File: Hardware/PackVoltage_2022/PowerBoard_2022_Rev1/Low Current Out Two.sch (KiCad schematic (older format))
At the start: 81 parts, among them Q10 BUK7M8R5-40HX, Q11 BUK7M8R5-40HX, Q12 BUK7M8R5-40HX, Q13 BUK7M8R5-40HX, Q14 BUK7M8R5-40HX, Q6 BUK7M8R5-40HX, Q7 BUK7M8R5-40HX, Q8 BUK7M8R5-40HX, Q9 BUK7M8R5-40HX, U22 LT1910, U23 LT1910, U24 LT1910, U25 LT1910, U26 INA281, U27 INA281, U28 INA281, U29 INA281, U30 INA281, U31 LT1910, U32 INA281, U33 LT1910, U34 LT1910, U35 LT1910, U36 LT1910, U37 INA281, U38 INA281, U39 INA281

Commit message: Made it to layout, found out about gnd via
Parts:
- renumbered C57 to C100, C58 to C101, C59 to C102, C60 to C103, C61 to C104, C62 to C105, C63 to C106, C64 to C107, C65 to C108, C66 to C109, C67 to C110, C50 to C93, C51 to C94, C52 to C95, C53 to C96, C54 to C97, C55 to C98, C56 to C99, D19 to D36, D20 to D37, D21 to D38, D22 to D39, D23 to D40, D24 to D41, D25 to D42, D26 to D43, D27 to D44, Q6 to Q14, Q7 to Q15, Q8 to Q16, Q9 to Q17, Q10 to Q18, Q11 to Q19, Q12 to Q20, Q13 to Q21, Q14 to Q22, R28 to R60, R29 to R61, R30 to R62, R31 to R63, R32 to R64, R33 to R65, R34 to R66, R35 to R67, R36 to R68, R37 to R69, R38 to R70, R39 to R71, R40 to R72, R41 to R73, R42 to R74, R43 to R75, R44 to R76, R45 to R77, R46 to R78, R47 to R79, R48 to R80, R49 to R81, R50 to R82, R51 to R83, R52 to R84, R53 to R85, R54 to R86, U22 to U48, U23 to U49, U24 to U50, U25 to U51, U26 to U52, U27 to U53, U28 to U54, U29 to U55, U30 to U56, U31 to U57, U32 to U58, U33 to U59, U34 to U60, U35 to U61, U36 to U62, U37 to U63, U38 to U64, U39 to U65

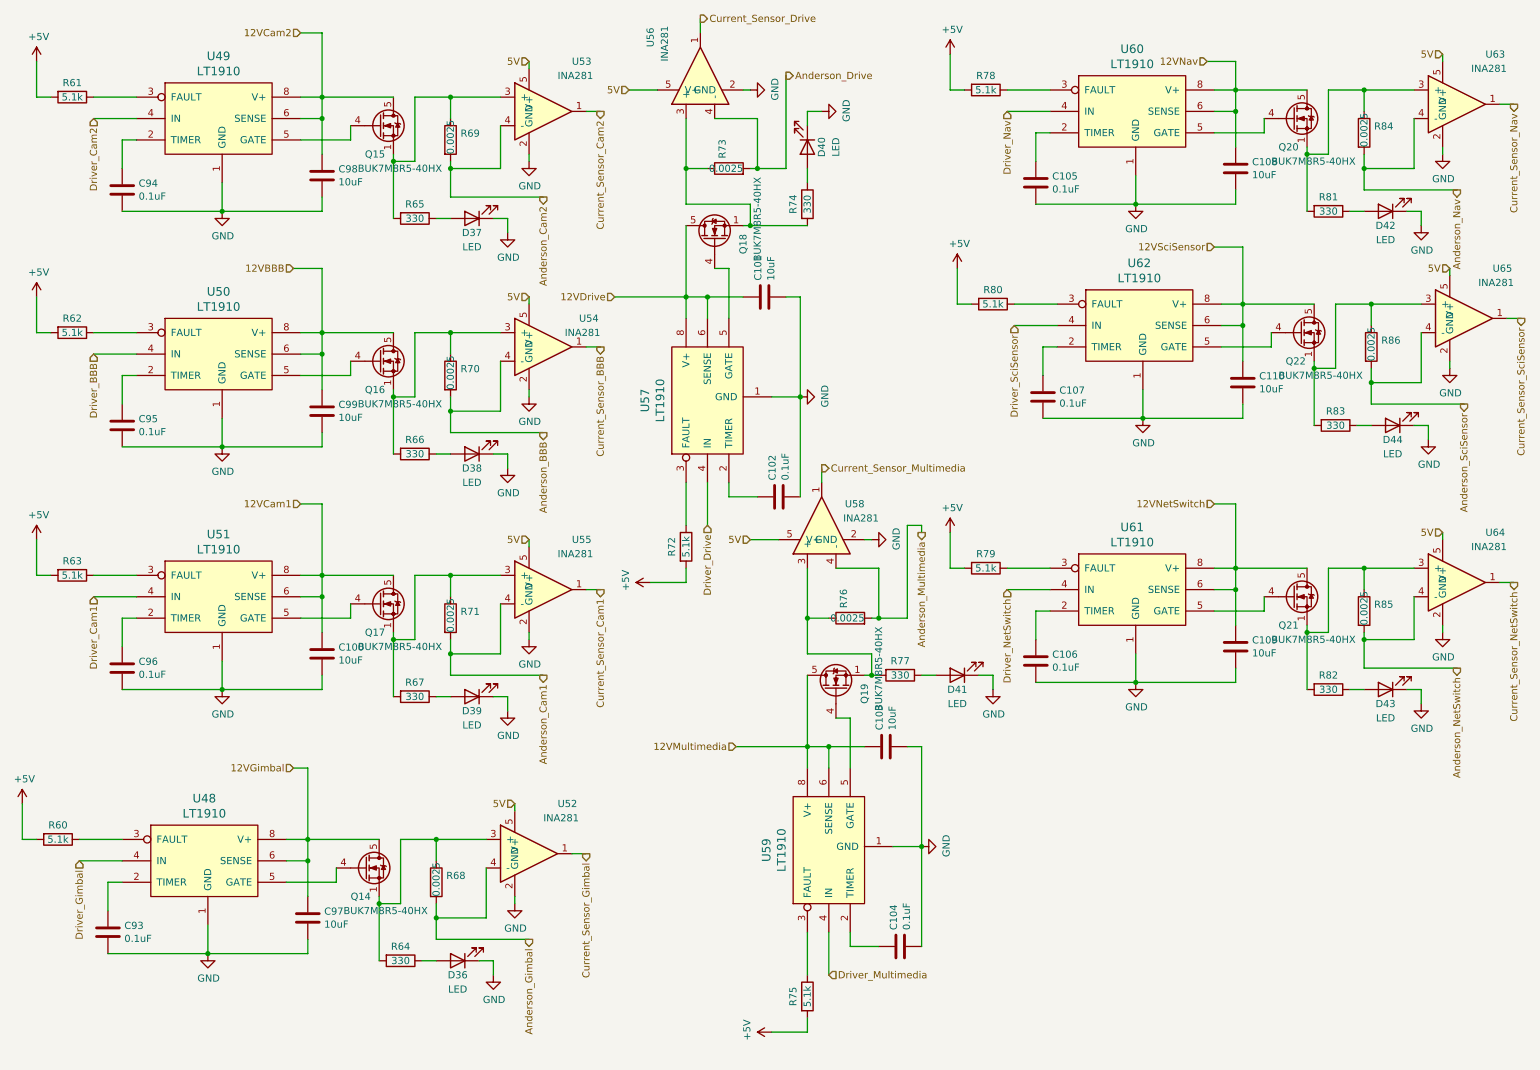
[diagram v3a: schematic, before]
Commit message: Organized  Stuff into groups and changed how we organize our board
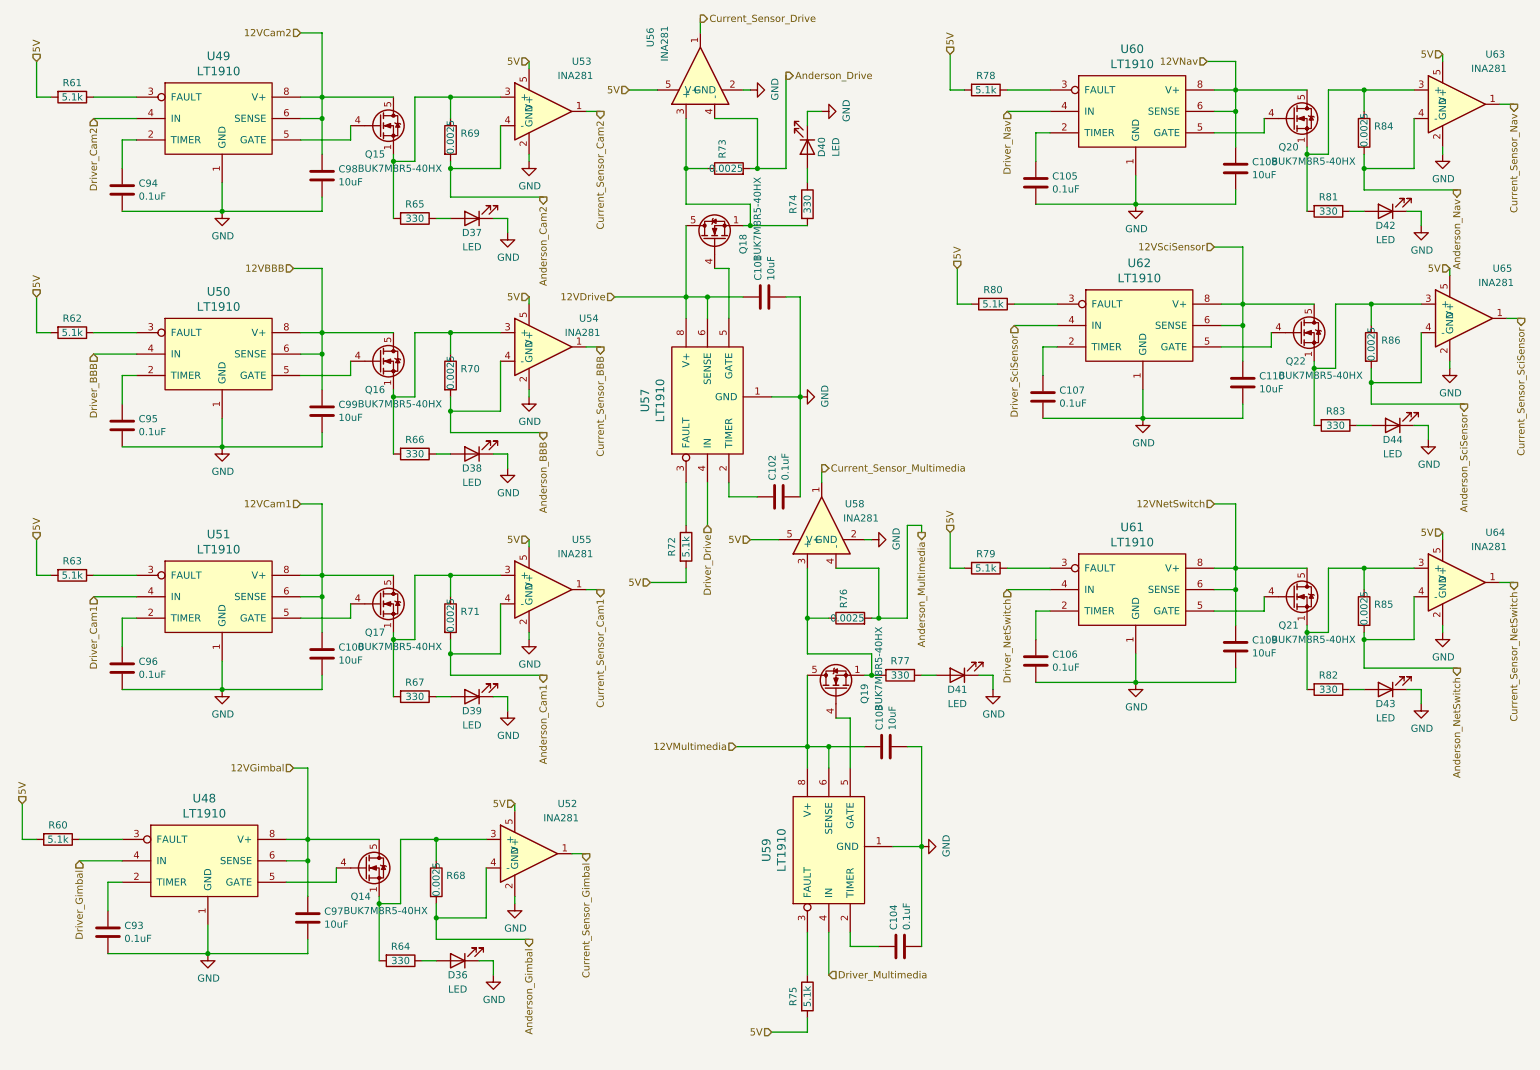
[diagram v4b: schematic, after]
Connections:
- net +5V is gone; now on net 5V: R60.2, R61.2, R62.2, R63.2, R72.2, R75.2, R78.2, R79.2, R80.2
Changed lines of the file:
@@
 EESchema Schematic File Version 4
-EELAYER 30 0
+LIBS:PowerBoard_2022_Rev1-cache
+EELAYER 26 0
 EELAYER END
 $Descr A4 11693 8268
@@
 Wire Wire Line
 	1100 2750 1400 2750
-$Comp
-L power:+5V #PWR?
-U 1 1 6179FA5B
-P 700 2500
-AR Path="/615D5992/6179FA5B" Ref="#PWR?"  Part="1"
-AR Path="/615D7BA0/6170B60A/6179FA5B" Ref="#PWR?"  Part="1"
-AR Path="/615D7BA0/6172F88A/6179FA5B" Ref="#PWR0124"  Part="1"
-F 0 "#PWR0124" H 700 2350 50  0001 C CNN
-F 1 "+5V" H 715 2673 50  0000 C CNN
-F 2 "" H 700 2500 50  0001 C CNN
-F 3 "" H 700 2500 50  0001 C CNN
-	1    700  2500
-	1    0    0    -1
-$EndComp
 Wire Wire Line
 	700  2500 700  2750
@@
 Wire Wire Line
 	1100 4450 1400 4450
-$Comp
-L power:+5V #PWR?
-U 1 1 6182162F
-P 700 4200
-AR Path="/615D5992/6182162F" Ref="#PWR?"  Part="1"
-AR Path="/615D7BA0/6170B60A/6182162F" Ref="#PWR?"  Part="1"
-AR Path="/615D7BA0/6172F88A/6182162F" Ref="#PWR0125"  Part="1"
-F 0 "#PWR0125" H 700 4050 50  0001 C CNN
-F 1 "+5V" H 715 4373 50  0000 C CNN
-F 2 "" H 700 4200 50  0001 C CNN
-F 3 "" H 700 4200 50  0001 C CNN
-	1    700  4200
-	1    0    0    -1
-$EndComp
 Wire Wire Line
 	700  4200 700  4450
@@
 Wire Wire Line
 	1100 1100 1400 1100
-$Comp
-L power:+5V #PWR?
-U 1 1 61833032
-P 700 850
-AR Path="/615D5992/61833032" Ref="#PWR?"  Part="1"
-AR Path="/615D7BA0/6170B60A/61833032" Ref="#PWR?"  Part="1"
-AR Path="/615D7BA0/6172F88A/61833032" Ref="#PWR0123"  Part="1"
-F 0 "#PWR0123" H 700 700 50  0001 C CNN
-F 1 "+5V" H 715 1023 50  0000 C CNN
-F 2 "" H 700 850 50  0001 C CNN
-F 3 "" H 700 850 50  0001 C CNN
-	1    700  850
-	1    0    0    -1
-$EndComp
 Wire Wire Line
 	700  850  700  1100
@@
 Wire Wire Line
 	7500 4400 7800 4400
-$Comp
-L power:+5V #PWR?
-U 1 1 61842604
-P 7100 4150
-AR Path="/615D5992/61842604" Ref="#PWR?"  Part="1"
-AR Path="/615D7BA0/6170B60A/61842604" Ref="#PWR?"  Part="1"
-AR Path="/615D7BA0/6172F88A/61842604" Ref="#PWR0146"  Part="1"
-F 0 "#PWR0146" H 7100 4000 50  0001 C CNN
-F 1 "+5V" H 7115 4323 50  0000 C CNN
-F 2 "" H 7100 4150 50  0001 C CNN
-F 3 "" H 7100 4150 50  0001 C CNN
-	1    7100 4150
-	1    0    0    -1
-$EndComp
 Wire Wire Line
 	7100 4150 7100 4400
@@
 Wire Wire Line
 	1000 6300 1300 6300
-$Comp
-L power:+5V #PWR?
-U 1 1 618D8DAA
-P 600 6050
-AR Path="/615D5992/618D8DAA" Ref="#PWR?"  Part="1"
-AR Path="/615D7BA0/6170B60A/618D8DAA" Ref="#PWR?"  Part="1"
-AR Path="/615D7BA0/6172F88A/618D8DAA" Ref="#PWR0122"  Part="1"
-F 0 "#PWR0122" H 600 5900 50  0001 C CNN
-F 1 "+5V" H 615 6223 50  0000 C CNN
-F 2 "" H 600 6050 50  0001 C CNN
-F 3 "" H 600 6050 50  0001 C CNN
-	1    600  6050
-	1    0    0    -1
-$EndComp
 Wire Wire Line
 	600  6050 600  6300
@@
 Wire Wire Line
 	7550 2550 7850 2550
-$Comp
-L power:+5V #PWR?
-U 1 1 61B8DD1A
-P 7150 2300
-AR Path="/615D5992/61B8DD1A" Ref="#PWR?"  Part="1"
-AR Path="/615D7BA0/6170B60A/61B8DD1A" Ref="#PWR?"  Part="1"
-AR Path="/615D7BA0/6172F88A/61B8DD1A" Ref="#PWR0147"  Part="1"
-F 0 "#PWR0147" H 7150 2150 50  0001 C CNN
-F 1 "+5V" H 7165 2473 50  0000 C CNN
-F 2 "" H 7150 2300 50  0001 C CNN
-F 3 "" H 7150 2300 50  0001 C CNN
-	1    7150 2300
-	1    0    0    -1
-$EndComp
 Wire Wire Line
 	7150 2300 7150 2550
@@
 Wire Wire Line
 	7500 1050 7800 1050
-$Comp
-L power:+5V #PWR?
-U 1 1 61BA276C
-P 7100 800
-AR Path="/615D5992/61BA276C" Ref="#PWR?"  Part="1"
-AR Path="/615D7BA0/6170B60A/61BA276C" Ref="#PWR?"  Part="1"
-AR Path="/615D7BA0/6172F88A/61BA276C" Ref="#PWR0145"  Part="1"
-F 0 "#PWR0145" H 7100 650 50  0001 C CNN
-F 1 "+5V" H 7115 973 50  0000 C CNN
-F 2 "" H 7100 800 50  0001 C CNN
-F 3 "" H 7100 800 50  0001 C CNN
-	1    7100 800
-	1    0    0    -1
-$EndComp
 Wire Wire Line
 	7100 800  7100 1050
@@
 Wire Wire Line
 	6100 7250 6100 6950
-$Comp
-L power:+5V #PWR?
-U 1 1 6209CF4A
-P 5850 7650
-AR Path="/615D5992/6209CF4A" Ref="#PWR?"  Part="1"
-AR Path="/61609A41/6209CF4A" Ref="#PWR?"  Part="1"
-AR Path="/615D7BA0/6172F88A/6209CF4A" Ref="#PWR0140"  Part="1"
-F 0 "#PWR0140" H 5850 7500 50  0001 C CNN
-F 1 "+5V" H 5865 7823 50  0000 C CNN
-F 2 "" H 5850 7650 50  0001 C CNN
-F 3 "" H 5850 7650 50  0001 C CNN
-	1    5850 7650
-	0    -1   -1   0
-$EndComp
 Wire Wire Line
 	5850 7650 6100 7650
@@
 Wire Wire Line
 	5250 4100 5250 3800
-$Comp
-L power:+5V #PWR?
-U 1 1 6219A363
-P 5000 4500
-AR Path="/615D5992/6219A363" Ref="#PWR?"  Part="1"
-AR Path="/61609A41/6219A363" Ref="#PWR?"  Part="1"
-AR Path="/615D7BA0/6172F88A/6219A363" Ref="#PWR0138"  Part="1"
-F 0 "#PWR0138" H 5000 4350 50  0001 C CNN
-F 1 "+5V" H 5015 4673 50  0000 C CNN
-F 2 "" H 5000 4500 50  0001 C CNN
-F 3 "" H 5000 4500 50  0001 C CNN
-	1    5000 4500
-	0    -1   -1   0
-$EndComp
 Wire Wire Line
 	5000 4500 5250 4500
@@
 Wire Wire Line
 	4750 2500 5250 2500
+Text HLabel 700  2500 1    50   Input ~ 0
+5V
+Text HLabel 700  850  1    50   Input ~ 0
+5V
+Text HLabel 700  4200 1    50   Input ~ 0
+5V
+Text HLabel 600  6050 1    50   Input ~ 0
+5V
+Text HLabel 5850 7650 0    50   Input ~ 0
+5V
+Text HLabel 5000 4500 0    50   Input ~ 0
+5V
+Text HLabel 7100 4150 1    50   Input ~ 0
+5V
+Text HLabel 7150 2300 1    50   Input ~ 0
+5V
+Text HLabel 7100 800  1    50   Input ~ 0
+5V
 $EndSCHEMATC

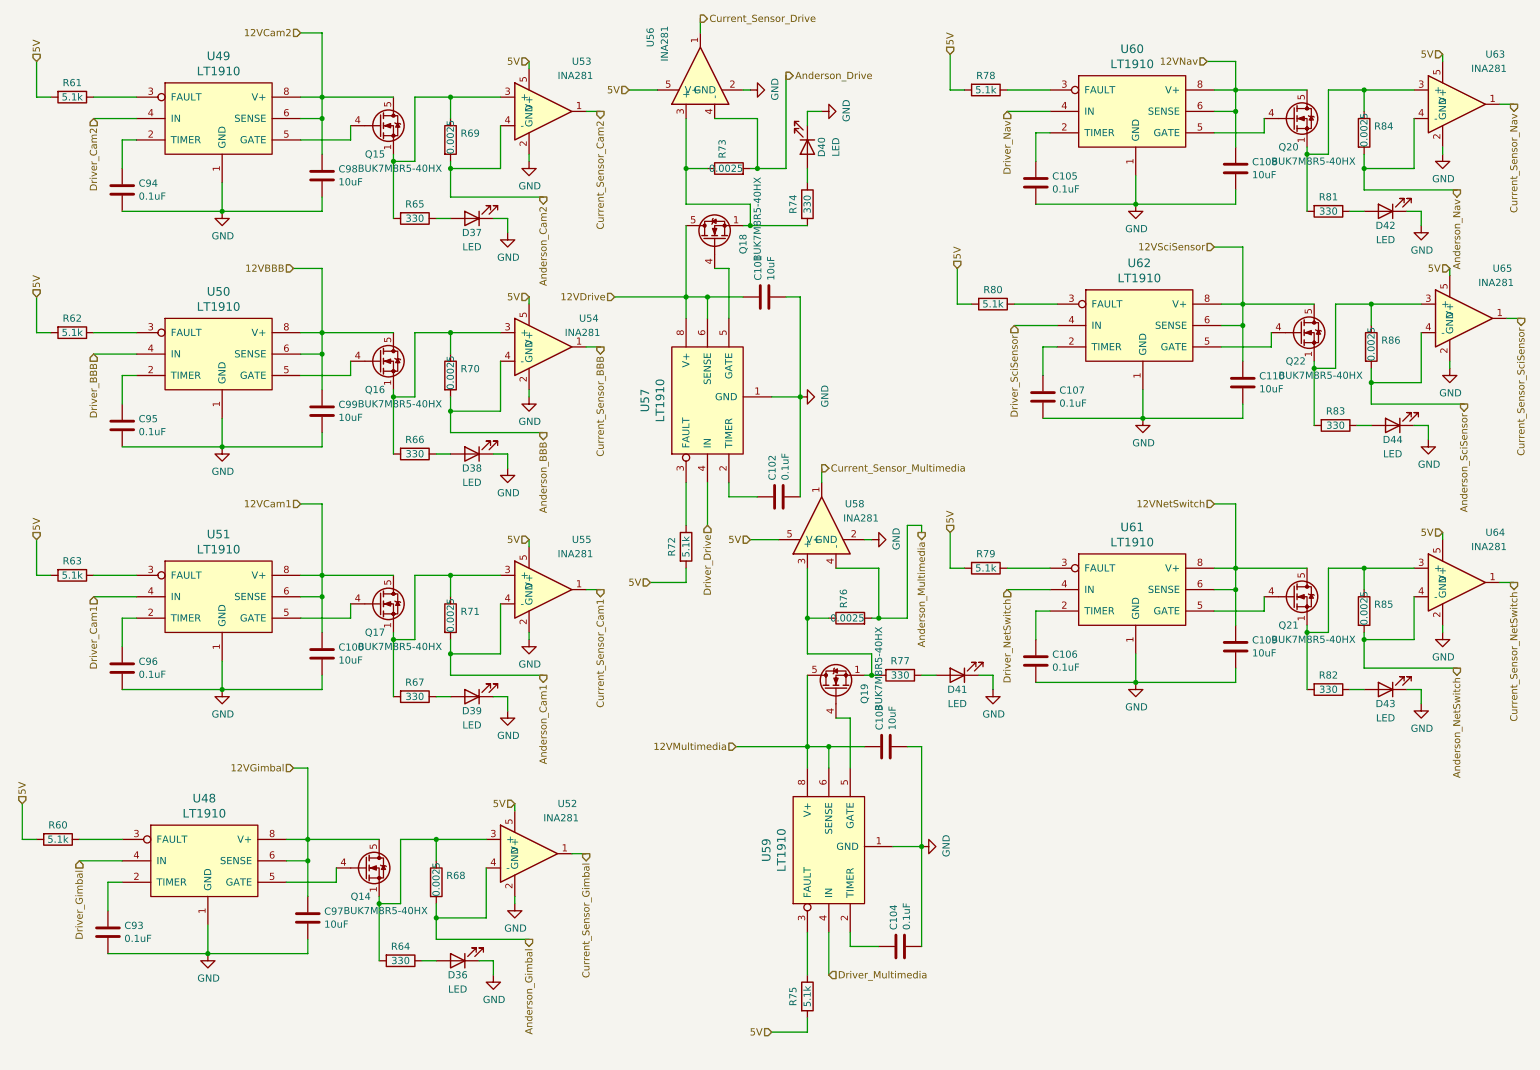
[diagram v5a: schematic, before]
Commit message: Removed redundant LED's in Actuation circuits and final touches on SciAct Layout
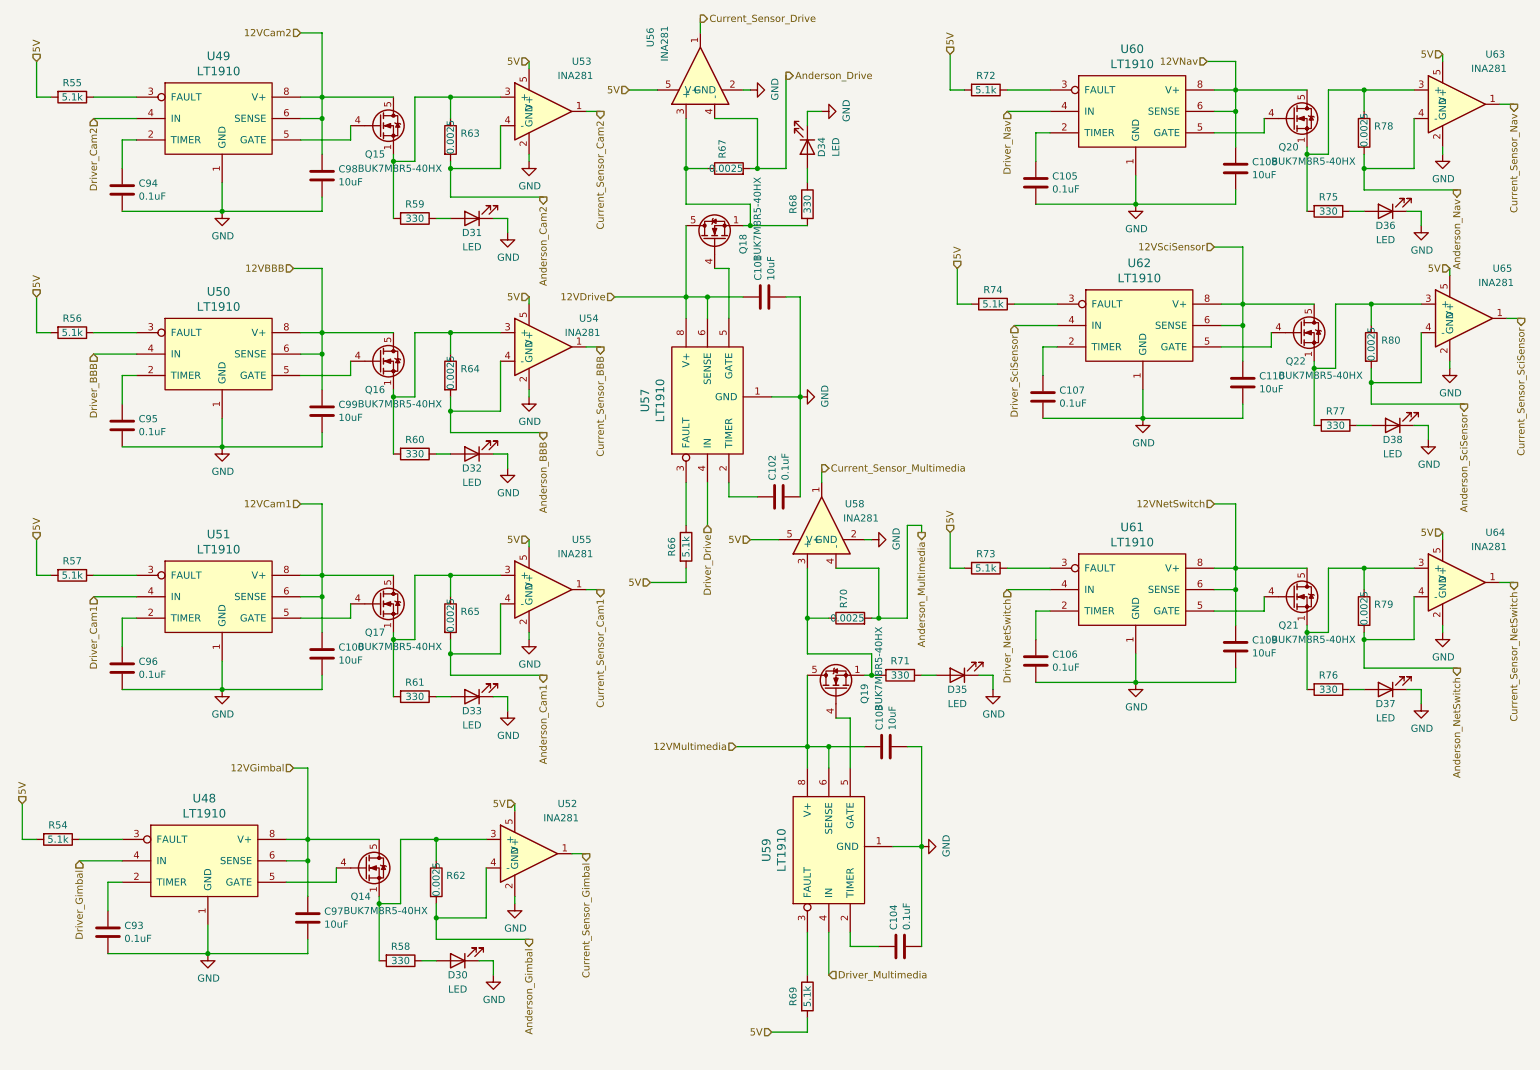
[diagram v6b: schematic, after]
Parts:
- renumbered D36 to D30, D37 to D31, D38 to D32, D39 to D33, D40 to D34, D41 to D35, D42 to D36, D43 to D37, D44 to D38, R60 to R54, R61 to R55, R62 to R56, R63 to R57, R64 to R58, R65 to R59, R66 to R60, R67 to R61, R68 to R62, R69 to R63, R70 to R64, R71 to R65, R72 to R66, R73 to R67, R74 to R68, R75 to R69, R76 to R70, R77 to R71, R78 to R72, R79 to R73, R80 to R74, R81 to R75, R82 to R76, R83 to R77, R84 to R78, R85 to R79, R86 to R80

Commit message: Replaced 12v okis w/big buck. Changed .0025 resistors to not 603.
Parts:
- R62, R63, R64, R65, R67, R70, R78, R79, R80: footprint Resistor_SMD:R_0603_1608Metric_Pad1.05x0.95mm_HandSolder -> Resistor_SMD:R_1206_3216Metric_Pad1.30x1.75mm_HandSolder
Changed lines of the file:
@@
 EESchema Schematic File Version 4
-LIBS:PowerBoard_2022_Rev1-cache
-EELAYER 26 0
+EELAYER 30 0
 EELAYER END
 $Descr A4 11693 8268
@@
 F 0 "R64" H 3670 3096 50  0000 L CNN
 F 1 "0.0025" V 3600 2950 50  0000 L CNN
-F 2 "Resistor_SMD:R_0603_1608Metric_Pad1.05x0.95mm_HandSolder" V 3530 3050 50  0001 C CNN
+F 2 "Resistor_SMD:R_1206_3216Metric_Pad1.30x1.75mm_HandSolder" V 3530 3050 50  0001 C CNN
 F 3 "~" H 3600 3050 50  0001 C CNN
 	1    3600 3050
@@
 F 0 "R65" H 3670 4796 50  0000 L CNN
 F 1 "0.0025" V 3600 4650 50  0000 L CNN
-F 2 "Resistor_SMD:R_0603_1608Metric_Pad1.05x0.95mm_HandSolder" V 3530 4750 50  0001 C CNN
+F 2 "Resistor_SMD:R_1206_3216Metric_Pad1.30x1.75mm_HandSolder" V 3530 4750 50  0001 C CNN
 F 3 "~" H 3600 4750 50  0001 C CNN
 	1    3600 4750
@@
 F 0 "R63" H 3670 1446 50  0000 L CNN
 F 1 "0.0025" V 3600 1300 50  0000 L CNN
-F 2 "Resistor_SMD:R_0603_1608Metric_Pad1.05x0.95mm_HandSolder" V 3530 1400 50  0001 C CNN
+F 2 "Resistor_SMD:R_1206_3216Metric_Pad1.30x1.75mm_HandSolder" V 3530 1400 50  0001 C CNN
 F 3 "~" H 3600 1400 50  0001 C CNN
 	1    3600 1400
@@
 F 0 "R79" H 10070 4746 50  0000 L CNN
 F 1 "0.0025" V 10000 4600 50  0000 L CNN
-F 2 "Resistor_SMD:R_0603_1608Metric_Pad1.05x0.95mm_HandSolder" V 9930 4700 50  0001 C CNN
+F 2 "Resistor_SMD:R_1206_3216Metric_Pad1.30x1.75mm_HandSolder" V 9930 4700 50  0001 C CNN
 F 3 "~" H 10000 4700 50  0001 C CNN
 	1    10000 4700
@@
 F 0 "R62" H 3570 6646 50  0000 L CNN
 F 1 "0.0025" V 3500 6500 50  0000 L CNN
-F 2 "Resistor_SMD:R_0603_1608Metric_Pad1.05x0.95mm_HandSolder" V 3430 6600 50  0001 C CNN
+F 2 "Resistor_SMD:R_1206_3216Metric_Pad1.30x1.75mm_HandSolder" V 3430 6600 50  0001 C CNN
 F 3 "~" H 3500 6600 50  0001 C CNN
 	1    3500 6600
@@
 F 0 "R80" H 10120 2896 50  0000 L CNN
 F 1 "0.0025" V 10050 2750 50  0000 L CNN
-F 2 "Resistor_SMD:R_0603_1608Metric_Pad1.05x0.95mm_HandSolder" V 9980 2850 50  0001 C CNN
+F 2 "Resistor_SMD:R_1206_3216Metric_Pad1.30x1.75mm_HandSolder" V 9980 2850 50  0001 C CNN
 F 3 "~" H 10050 2850 50  0001 C CNN
 	1    10050 2850
@@
 F 0 "R78" H 10070 1396 50  0000 L CNN
 F 1 "0.0025" V 10000 1250 50  0000 L CNN
-F 2 "Resistor_SMD:R_0603_1608Metric_Pad1.05x0.95mm_HandSolder" V 9930 1350 50  0001 C CNN
+F 2 "Resistor_SMD:R_1206_3216Metric_Pad1.30x1.75mm_HandSolder" V 9930 1350 50  0001 C CNN
 F 3 "~" H 10000 1350 50  0001 C CNN
 	1    10000 1350
@@
 F 0 "R70" H 6470 4796 50  0000 L CNN
 F 1 "0.0025" V 6400 4650 50  0000 L CNN
-F 2 "Resistor_SMD:R_0603_1608Metric_Pad1.05x0.95mm_HandSolder" V 6330 4750 50  0001 C CNN
+F 2 "Resistor_SMD:R_1206_3216Metric_Pad1.30x1.75mm_HandSolder" V 6330 4750 50  0001 C CNN
 F 3 "~" H 6400 4750 50  0001 C CNN
 	1    6400 4750
@@
 F 0 "R67" H 5620 1646 50  0000 L CNN
 F 1 "0.0025" V 5550 1500 50  0000 L CNN
-F 2 "Resistor_SMD:R_0603_1608Metric_Pad1.05x0.95mm_HandSolder" V 5480 1600 50  0001 C CNN
+F 2 "Resistor_SMD:R_1206_3216Metric_Pad1.30x1.75mm_HandSolder" V 5480 1600 50  0001 C CNN
 F 3 "~" H 5550 1600 50  0001 C CNN
 	1    5550 1600
